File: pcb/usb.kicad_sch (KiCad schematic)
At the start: 8 parts, among them J2 Same Sky UJ20-C-H-G-SMT-P16-TR, U2 USBLC6-2SC6

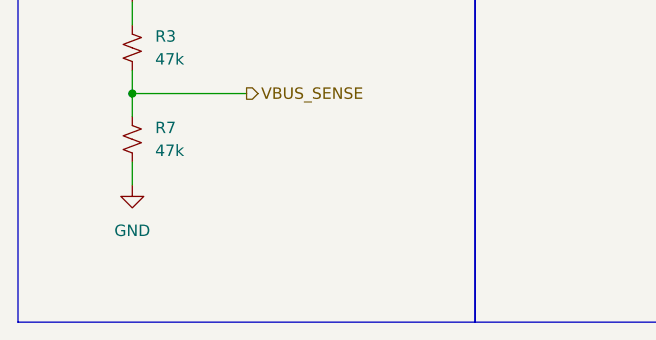
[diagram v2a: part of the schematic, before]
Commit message: Implement flash memory connection
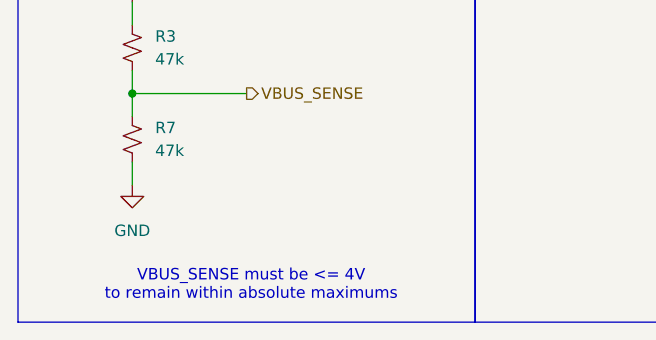
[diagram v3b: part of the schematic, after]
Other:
- note added: "VBUS_SENSE must be <= 4V to remain within absolute maximums"
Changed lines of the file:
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@@
+		)
+	)
+	(text "VBUS_SENSE must be <= 4V\nto remain within absolute maximums"
+		(exclude_from_sim no)
+		(at 38.608 148.336 0)
+		(effects
+			(font
+				(size 1.27 1.27)
+			)
 		)
 	)

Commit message: Update project
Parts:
- R3: value 47k -> 30k
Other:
- note added: "or 47k would probably work fine too"
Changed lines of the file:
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@@
+		)
+	)
+	(text "or 47k would probably work fine too"
+		(exclude_from_sim no)
+		(at 44.45 117.348 0)
+		(effects
+			(font
+				(size 1.27 1.27)
+			)
 		)
 	)
@@
 			)
 		)
-		(property "Value" "47k"
+		(property "Value" "30k"
 			(at 27.94 123.1899 0)
 			(effects

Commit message: Start layout
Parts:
- R15: renamed from R3; footprint (none) -> Resistor_SMD:R_0603_1608Metric
- R16: renamed from R7; footprint (none) -> Resistor_SMD:R_0603_1608Metric
- renumbered D1 to D2, R4 to R17, R5 to R18, R6 to R19, U2 to U4
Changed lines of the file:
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@@
 		(dnp no)
 		(fields_autoplaced yes)
-		(property "Reference" "#PWR025"
+		(property "Reference" "#PWR045"
 			(at 25.4 143.51 0)
 			(effects
@@
 			(project ""
 				(path "/1f4fd4ed-9886-4375-a5ac-dc32d5760936/ca842921-3489-4085-9fee-8380a44600c3"
-					(reference "#PWR025")
+					(reference "#PWR045")
 					(unit 1)
 				)
@@
 		(on_board yes)
 		(dnp no)
-		(property "Reference" "#PWR033"
+		(property "Reference" "#PWR047"
 			(at 69.85 87.63 0)
 			(effects
@@
 			(project "airbrake_mod"
 				(path "/1f4fd4ed-9886-4375-a5ac-dc32d5760936/ca842921-3489-4085-9fee-8380a44600c3"
-					(reference "#PWR033")
+					(reference "#PWR047")
 					(unit 1)
 				)
@@
 		(dnp no)
 		(fields_autoplaced yes)
-		(property "Reference" "R6"
+		(property "Reference" "R19"
 			(at 91.44 121.9199 0)
 			(effects
@@
 			(project "airbrake_mod"
 				(path "/1f4fd4ed-9886-4375-a5ac-dc32d5760936/ca842921-3489-4085-9fee-8380a44600c3"
-					(reference "R6")
+					(reference "R19")
 					(unit 1)
 				)
@@
 		(on_board yes)
 		(dnp no)
-		(property "Reference" "R4"
+		(property "Reference" "R17"
 			(at 58.42 40.894 90)
 			(effects
@@
 			(project "airbrake_mod"
 				(path "/1f4fd4ed-9886-4375-a5ac-dc32d5760936/ca842921-3489-4085-9fee-8380a44600c3"
-					(reference "R4")
+					(reference "R17")
 					(unit 1)
 				)
@@
 		(dnp no)
 		(fields_autoplaced yes)
-		(property "Reference" "#PWR032"
+		(property "Reference" "#PWR051"
 			(at 88.9 142.24 0)
 			(effects
@@
 			(project "airbrake_mod"
 				(path "/1f4fd4ed-9886-4375-a5ac-dc32d5760936/ca842921-3489-4085-9fee-8380a44600c3"
-					(reference "#PWR032")
+					(reference "#PWR051")
 					(unit 1)
 				)
@@
 		(dnp no)
 		(fields_autoplaced yes)
-		(property "Reference" "D1"
+		(property "Reference" "D2"
 			(at 91.44 129.4764 90)
 			(effects
@@
 			(project "airbrake_mod"
 				(path "/1f4fd4ed-9886-4375-a5ac-dc32d5760936/ca842921-3489-4085-9fee-8380a44600c3"
-					(reference "D1")
+					(reference "D2")
 					(unit 1)
 				)
@@
 		(dnp no)
 		(fields_autoplaced yes)
-		(property "Reference" "#PWR024"
+		(property "Reference" "#PWR044"
 			(at 25.4 120.65 0)
 			(effects
@@
 			(project "airbrake_mod"
 				(path "/1f4fd4ed-9886-4375-a5ac-dc32d5760936/ca842921-3489-4085-9fee-8380a44600c3"
-					(reference "#PWR024")
+					(reference "#PWR044")
 					(unit 1)
 				)
@@
 		(dnp no)
 		(fields_autoplaced yes)
-		(property "Reference" "#PWR029"
+		(property "Reference" "#PWR048"
 			(at 88.9 39.37 0)
 			(effects
@@
 			(project "airbrake_mod"
 				(path "/1f4fd4ed-9886-4375-a5ac-dc32d5760936/ca842921-3489-4085-9fee-8380a44600c3"
-					(reference "#PWR029")
+					(reference "#PWR048")
 					(unit 1)
 				)
@@
 		(on_board yes)
 		(dnp no)
-		(property "Reference" "R5"
+		(property "Reference" "R18"
 			(at 58.674 48.006 90)
 			(effects
@@
 			(project "airbrake_mod"
 				(path "/1f4fd4ed-9886-4375-a5ac-dc32d5760936/ca842921-3489-4085-9fee-8380a44600c3"
-					(reference "R5")
+					(reference "R18")
 					(unit 1)
 				)
@@
 		(dnp no)
 		(fields_autoplaced yes)
-		(property "Reference" "R3"
+		(property "Reference" "R15"
 			(at 27.94 120.6499 0)
 			(effects
@@
 			)
 		)
-		(property "Footprint" ""
+		(property "Footprint" "Resistor_SMD:R_0603_1608Metric"
 			(at 25.4 121.92 0)
 			(effects
@@
 			(project ""
 				(path "/1f4fd4ed-9886-4375-a5ac-dc32d5760936/ca842921-3489-4085-9fee-8380a44600c3"
-					(reference "R3")
+					(reference "R15")
 					(unit 1)
 				)
@@
 		(dnp no)
 		(fields_autoplaced yes)
-		(property "Reference" "U2"
+		(property "Reference" "U4"
 			(at 90.5511 45.72 0)
 			(effects
@@
 			(project "airbrake_mod"
 				(path "/1f4fd4ed-9886-4375-a5ac-dc32d5760936/ca842921-3489-4085-9fee-8380a44600c3"
-					(reference "U2")
+					(reference "U4")
 					(unit 1)
 				)
@@
 		(dnp no)
 		(fields_autoplaced yes)
-		(property "Reference" "#PWR031"
+		(property "Reference" "#PWR050"
 			(at 88.9 121.92 0)
 			(effects
@@
 			(project "airbrake_mod"
 				(path "/1f4fd4ed-9886-4375-a5ac-dc32d5760936/ca842921-3489-4085-9fee-8380a44600c3"
-					(reference "#PWR031")
+					(reference "#PWR050")
 					(unit 1)
 				)
@@
 		(dnp no)
 		(fields_autoplaced yes)
-		(property "Reference" "#PWR030"
+		(property "Reference" "#PWR049"
 			(at 88.9 87.63 0)
 			(effects
@@
 			(project "airbrake_mod"
 				(path "/1f4fd4ed-9886-4375-a5ac-dc32d5760936/ca842921-3489-4085-9fee-8380a44600c3"
-					(reference "#PWR030")
+					(reference "#PWR049")
 					(unit 1)
 				)
@@
 		(dnp no)
 		(fields_autoplaced yes)
-		(property "Reference" "R7"
+		(property "Reference" "R16"
 			(at 27.94 130.8099 0)
 			(effects
@@
 			)
 		)
-		(property "Footprint" ""
+		(property "Footprint" "Resistor_SMD:R_0603_1608Metric"
 			(at 25.4 132.08 0)
 			(effects
@@
 			(project "airbrake_mod"
 				(path "/1f4fd4ed-9886-4375-a5ac-dc32d5760936/ca842921-3489-4085-9fee-8380a44600c3"
-					(reference "R7")
+					(reference "R16")
 					(unit 1)
 				)
@@
 		(dnp no)
 		(fields_autoplaced yes)
-		(property "Reference" "#PWR026"
+		(property "Reference" "#PWR046"
 			(at 35.56 87.63 0)
 			(effects
@@
 			(project "airbrake_mod"
 				(path "/1f4fd4ed-9886-4375-a5ac-dc32d5760936/ca842921-3489-4085-9fee-8380a44600c3"
-					(reference "#PWR026")
-					(unit 1)
-				)
+					(reference "#PWR046")
+					(unit 1)
+				)

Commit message: Layout power
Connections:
- net USB_D+: now also J2.A6 (D+), J2.B6 (D+), U4.3 (I/O2)
- net USB_D-: now also J2.A7 (D-), J2.B7 (D-), U4.1 (I/O1)
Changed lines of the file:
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@@
+		)
+	)
+	(label "USB_D+"
+		(at 53.34 58.42 0)
+		(effects
+			(font
+				(size 1.27 1.27)
+			)
+			(justify left bottom)
+		)
+	)
+	(label "USB_D-"
+		(at 53.34 53.34 0)
+		(effects
+			(font
+				(size 1.27 1.27)
+			)
+			(justify left bottom)
 		)
 	)

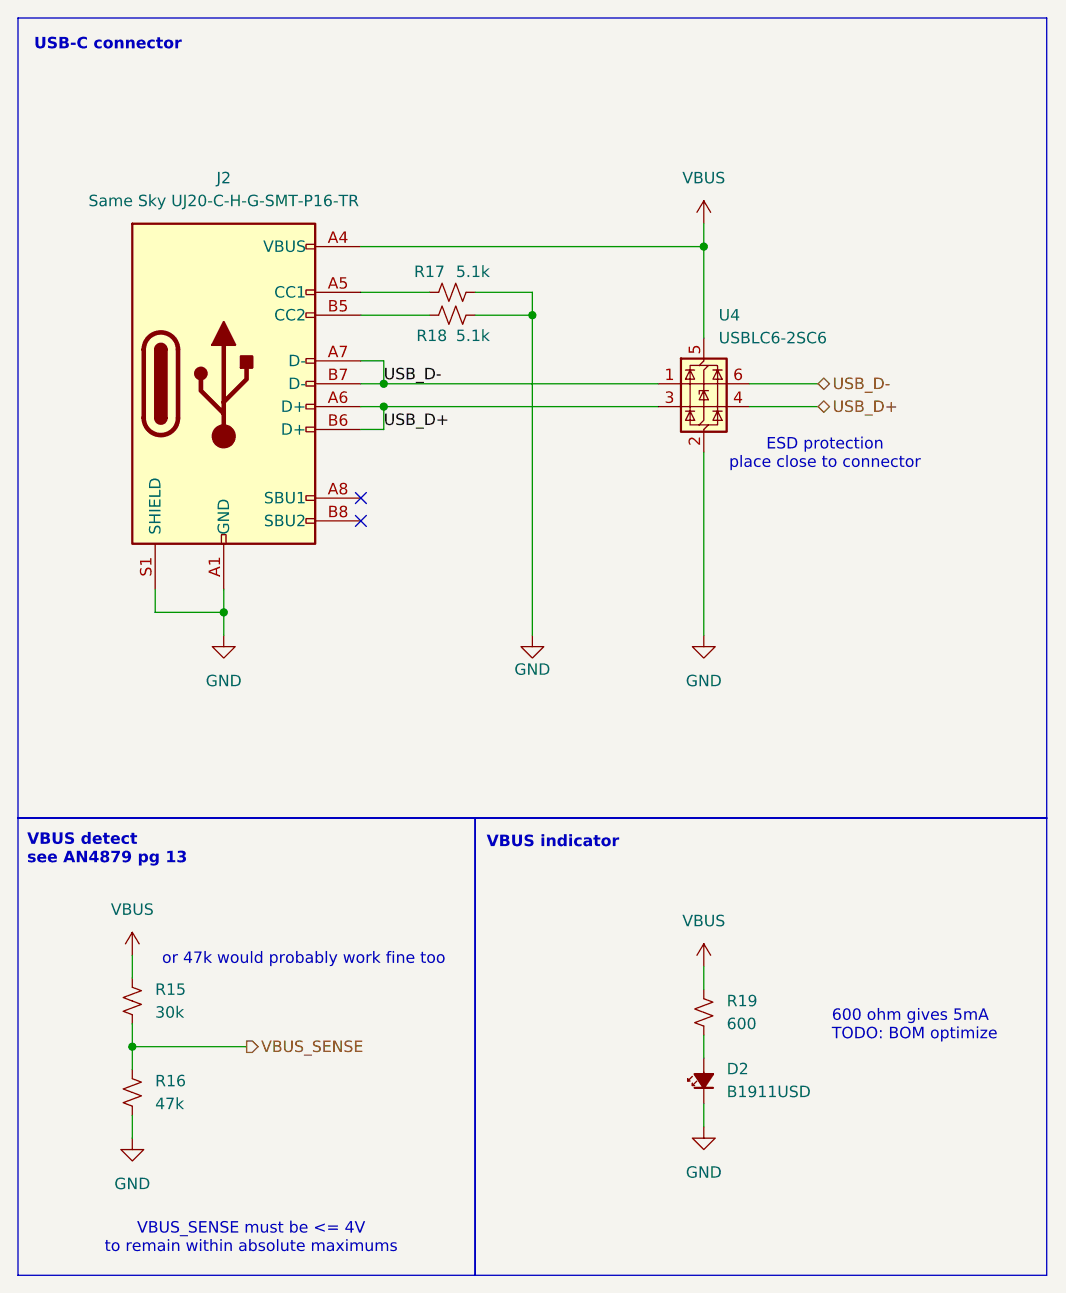
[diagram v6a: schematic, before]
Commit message: Layout MCU decoupling
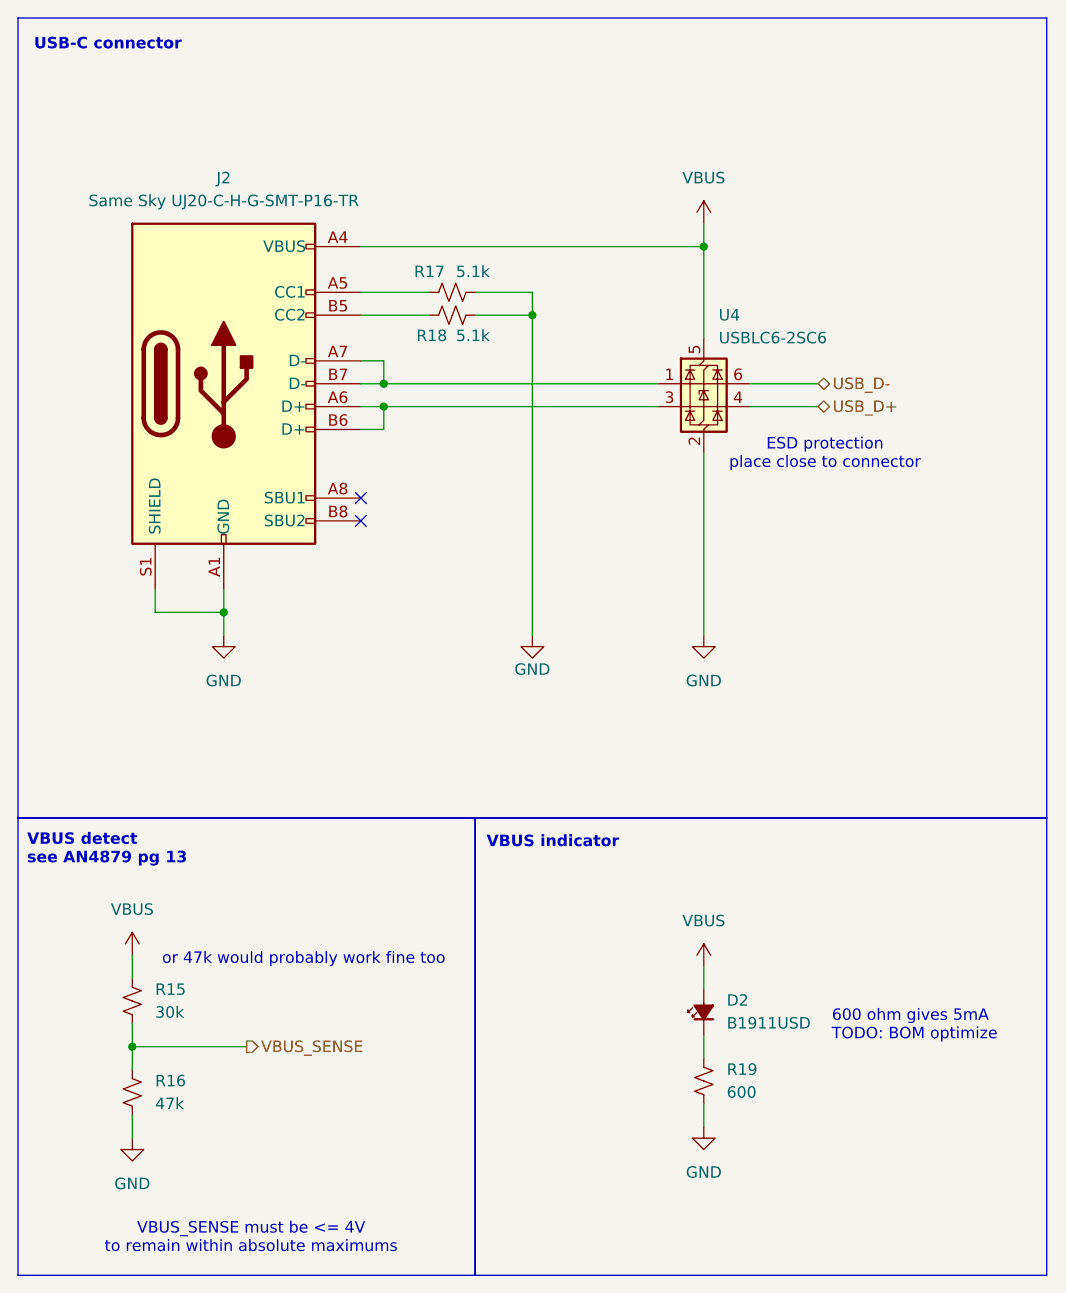
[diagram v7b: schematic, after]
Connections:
- net GND: now also R19.2; no longer D2.1 (K)
- net USB_D+: no longer J2.A6 (D+), J2.B6 (D+), U4.3 (I/O2)
- net USB_D-: no longer J2.A7 (D-), J2.B7 (D-), U4.1 (I/O1)
- net VBUS: now also D2.2 (A); no longer R19.1
- new net: D2.1 (K), R19.1
- new net: J2.A6 (D+), J2.B6 (D+), U4.3 (I/O2)
- new net: J2.A7 (D-), J2.B7 (D-), U4.1 (I/O1)
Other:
- moved on the sheet: D2, R19
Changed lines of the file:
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@@
-		)
-	)
-	(label "USB_D+"
-		(at 53.34 58.42 0)
-		(effects
-			(font
-				(size 1.27 1.27)
-			)
-			(justify left bottom)
-		)
-	)
-	(label "USB_D-"
-		(at 53.34 53.34 0)
-		(effects
-			(font
-				(size 1.27 1.27)
-			)
-			(justify left bottom)
 		)
 	)
@@
 	(symbol
 		(lib_id "Device:R_Small_US")
-		(at 88.9 123.19 0)
+		(at 88.9 130.81 0)
 		(unit 1)
 		(exclude_from_sim no)
@@
 		(fields_autoplaced yes)
 		(property "Reference" "R19"
-			(at 91.44 121.9199 0)
+			(at 91.44 129.5399 0)
 			(effects
 				(font
@@
 		)
 		(property "Value" "600"
-			(at 91.44 124.4599 0)
+			(at 91.44 132.0799 0)
 			(effects
 				(font
@@
 		)
 		(property "Footprint" "Resistor_SMD:R_0603_1608Metric"
-			(at 88.9 123.19 0)
+			(at 88.9 130.81 0)
 			(effects
 				(font
@@
 		)
 		(property "Datasheet" "~"
-			(at 88.9 123.19 0)
+			(at 88.9 130.81 0)
 			(effects
 				(font
@@
 		)
 		(property "Description" "Resistor, small US symbol"
-			(at 88.9 123.19 0)
+			(at 88.9 130.81 0)
 			(effects
 				(font
@@
 	(symbol
 		(lib_id "Device:LED_Small_Filled")
-		(at 88.9 130.81 90)
+		(at 88.9 123.19 90)
 		(unit 1)
 		(exclude_from_sim no)
@@
 		(fields_autoplaced yes)
 		(property "Reference" "D2"
-			(at 91.44 129.4764 90)
+			(at 91.44 121.8564 90)
 			(effects
 				(font
@@
 		)
 		(property "Value" "B1911USD"
-			(at 91.44 132.0164 90)
+			(at 91.44 124.3964 90)
 			(effects
 				(font
@@
 		)
 		(property "Footprint" "LED_SMD:LED_0603_1608Metric"
-			(at 88.9 130.81 90)
+			(at 88.9 123.19 90)
 			(effects
 				(font
@@
 		)
 		(property "Datasheet" "~"
-			(at 88.9 130.81 90)
+			(at 88.9 123.19 90)
 			(effects
 				(font
@@
 		)
 		(property "Description" "Light emitting diode, small symbol, filled shape"
-			(at 88.9 130.81 0)
+			(at 88.9 123.19 0)
 			(effects
 				(font
@@
 		)
 		(property "Sim.Pins" "1=K 2=A"
-			(at 88.9 130.81 0)
-			(effects
-				(font
+			(at 88.9 123.19 0)
+			(effects
+				(font
